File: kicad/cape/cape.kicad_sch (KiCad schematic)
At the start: 13 parts, among them M1 HSR-2648CR, P1 BeagleBone_Black_Header, P2 BeagleBone_Black_Header, SW1 L101011_SPST, U1 L298, U2 BNO055, U3 BMP390, U4 S13V10FS

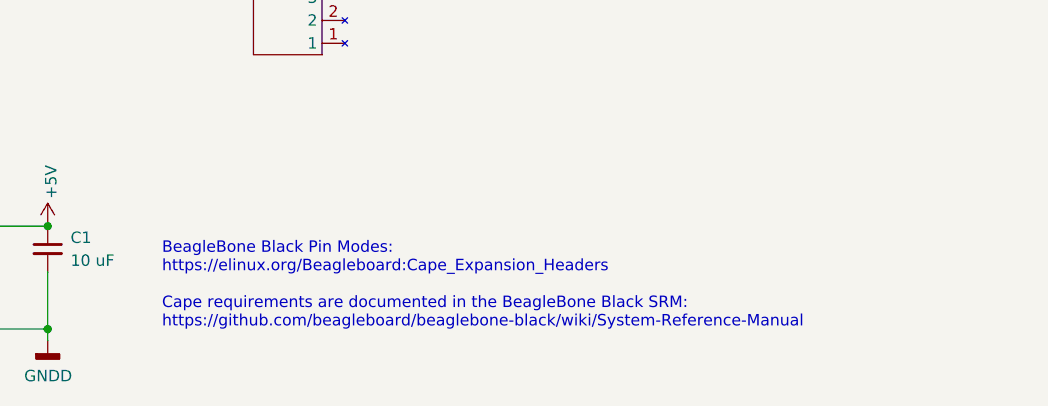
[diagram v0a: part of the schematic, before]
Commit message: Moved cape pdf files to doc
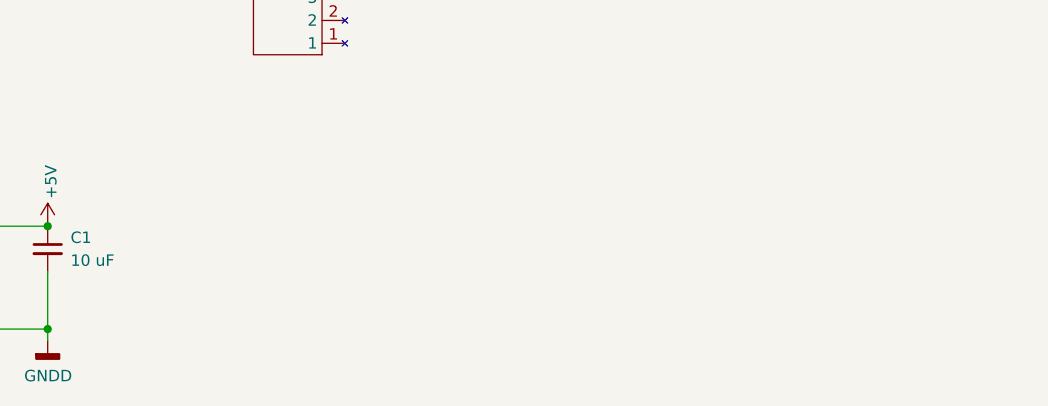
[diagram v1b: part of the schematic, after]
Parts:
- U1: footprint Connector_PinSocket_2.54mm:PinSocket_1x06_P2.54mm_Vertical -> Connector_PinHeader_2.54mm:PinHeader_1x06_P2.54mm_Vertical
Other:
- note removed: "BeagleBone Black Pin Modes: https://elinux.org/Beagleboard:Cape_Expansion_Headers Cape requirements are documented in the BeagleBone Black SRM: https://github.com/beagleboard/beaglebone-black/wiki/System-Reference-Manual"
- title: (none) -> Payload BeagleBone Black Cape
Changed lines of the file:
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@@
 (kicad_sch (version 20211123) (generator eeschema)
   (paper "A4")
+  (title_block
+    (title "Payload BeagleBone Black Cape")
+    (date "2022-12-18")
+    (rev "1.1")
+  )
   (junction (at 134.62 180.34) (diameter 0) (color 0 0 0 0)
   )
@@
     (stroke (width 0) (type default) (color 0 0 0 0))
   )
-  (text "BeagleBone Black Pin Modes:\nhttps://elinux.org/Beagleboard:Cape_Expansion_Headers\n\nCape requirements are documented in the BeagleBone Black SRM:\nhttps://github.com/beagleboard/beaglebone-black/wiki/System-Reference-Manual"
-    (at 177.8 180.34 0)
+  (text "\n" (at 177.8 180.34 0)
     (effects (font (size 1.27 1.27)) (justify left bottom))
   )
@@
     (property "Reference" "U1" (id 0) (at 66.04 124.46 0))
     (property "Value" "L298" (id 1) (at 66.04 127 0))
-    (property "Footprint" "Connector_PinSocket_2.54mm:PinSocket_1x06_P2.54mm_Vertical" (id 2) (at 55.88 129.54 0)
+    (property "Footprint" "Connector_PinHeader_2.54mm:PinHeader_1x06_P2.54mm_Vertical" (id 2) (at 55.88 129.54 0)
       (effects (font (size 1.27 1.27)) hide)
     )
@@
     )
     (path "/ecf7c526-1bd5-49c8-a82a-8acc85e22ee0"
-      (reference "U1") (unit 1) (value "L298") (footprint "Connector_PinSocket_2.54mm:PinSocket_1x06_P2.54mm_Vertical")
+      (reference "U1") (unit 1) (value "L298") (footprint "Connector_PinHeader_2.54mm:PinHeader_1x06_P2.54mm_Vertical")
     )
     (path "/ae4a70ec-7099-49d5-8f39-6daa3b0242a8"

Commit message: Cape v 1.2
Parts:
- removed H1: GPIO_Breakout, Connector_PinHeader_2.54mm:PinHeader_1x08_P2.54mm_Vertical, symbol payload_symbol_library:GPIO_Breakout
- removed U1: L298, Connector_PinHeader_2.54mm:PinHeader_1x06_P2.54mm_Vertical, symbol payload_symbol_library:L298
- removed U3: BMP390, payload_footprint_library:BMP390, symbol payload_symbol_library:BMP390
- added C1: 100 uF, Capacitor_THT:C_Radial_D10.0mm_H16.0mm_P5.00mm, symbol Device:C_Small
- added U3: A4988, payload_footprint_library:Pololu_Breakout-16_15.2x20.3mm, symbol payload_symbol_library:A4988
- C2: renamed from C1; value 10 uF -> 10 nF; footprint Capacitor_THT:C_Radial_D10.0mm_H16.0mm_P5.00mm -> Capacitor_THT:C_Disc_D10.0mm_W2.5mm_P5.00mm
- M1: footprint Connector_PinHeader_2.54mm:PinHeader_1x03_P2.54mm_Vertical -> Connector_PinSocket_2.54mm:PinSocket_1x03_P2.54mm_Vertical
- SW1: footprint payload_footprint_library:SPST -> payload_footprint_library:SW_L101011MS02Q
- U1: renamed from U4; value S13V10FS -> S13V10F5; symbol payload_symbol_library:S13V10FS -> payload_symbol_library:S13V10F5
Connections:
- net +3.3V: now also U3.2 (VDD)
- net +7.4V: now also C1.1, U3.8 (VMOT)
- net GNDD: now also C1.2, U3.1 (GND), U3.7 (GND)
- net GPIO[117]: now also U2.6 (RST)
- net GPIO[20]: no longer U2.6 (RST)
- net GPIO[27]: now also U3.14 (~{SLEEP})
- net GPIO[47]: now also U3.13 (~{RESET})
- net GPIO[61]: now also U3.16 (DIR)
- net GPIO[65]: now also U3.15 (STEP)
- net I2C2.SCL: now also R2.2; no longer R1.2
- net I2C2.SDA: now also R1.2; no longer R2.2
- net GPIO[122] renamed GPIO_112
- net GPIO_112: now also U2.9 (INT)
- net GPIO[125] renamed GPIO_115
- no-connect marks 0 -> 12
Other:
- moved on the sheet: BT1, C2, M1, P1, P2, SW1, U1

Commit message: Cape 1.3, Main 1.7
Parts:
- added C3: 100 uF, Capacitor_THT:C_Radial_D10.0mm_H16.0mm_P5.00mm, symbol Device:C_Small
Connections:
- net +5V: now also C3.1
- net GNDD: now also C3.2
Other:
- moved on the sheet: BT1, C1, C2, M1, P1, P2, R1, R2, SW1, U1, U2, U3

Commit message: Updated all schematics
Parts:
- removed SW1: L101011_SPST, payload_footprint_library:SW_L101011MS02Q, symbol Switch:SW_SPST
- added JP1: Jumper_3_Open, Connector_PinHeader_2.54mm:PinHeader_1x03_P2.54mm_Vertical, symbol Jumper:Jumper_3_Open
- added U3: stepper_breakout, Connector_PinSocket_2.54mm:PinSocket_1x04_P2.54mm_Vertical, symbol payload_symbol_library:stepper_breakout
- renumbered U2 to U1, U1 to U2, U3 to U4
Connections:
- net +7.4V: now also JP1.3 (B)
- net at BT1.1 (+): now also JP1.2 (C)
- net at U4.3 (1B): now also U3.1 (1B)
- net at U4.4 (1A): now also U3.2 (1A)
- net at U4.5 (2A): now also U3.3 (2A)
- net at U4.6 (2B): now also U3.4 (2B)
- no-connect marks 12 -> 9
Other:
- company: (none) -> Peter Costescu
- moved on the sheet: U4

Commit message: Exported gerber to JLC PCB
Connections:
- net GPIO[61]: now also P2.26 (Pin_26); no longer P2.28 (Pin_28)
- net LCD.PCLK: now also P2.28 (Pin_28); no longer P2.26 (Pin_26)
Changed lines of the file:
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@@
+    (effects (font (size 1.27 1.27)) (justify right bottom))
+  )
+  (label "LCD.PCLK" (at 129.54 60.96 180)
     (effects (font (size 1.27 1.27)) (justify right bottom))
   )
@@
     (effects (font (size 1.27 1.27)) (justify left bottom))
   )
-  (label "LCD.PCLK" (at 129.54 58.42 180)
-    (effects (font (size 1.27 1.27)) (justify right bottom))
-  )
   (label "GPIO[44]" (at 129.54 40.64 180)
     (effects (font (size 1.27 1.27)) (justify right bottom))
@@
     (effects (font (size 1.27 1.27)) (justify left bottom))
   )
-  (label "GPIO[61]" (at 129.54 60.96 180)
-    (effects (font (size 1.27 1.27)) (justify right bottom))
-  )
   (label "GPIO_112" (at 67.31 63.5 180)
     (effects (font (size 1.27 1.27)) (justify right bottom))
@@
     (effects (font (size 1.27 1.27)) (justify right bottom))
   )
+  (label "GPIO[61]" (at 129.54 58.42 180)
+    (effects (font (size 1.27 1.27)) (justify right bottom))
+  )

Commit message: Working on post-build payload changes
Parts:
- removed U3: stepper_breakout, Connector_PinSocket_2.54mm:PinSocket_1x04_P2.54mm_Vertical, symbol payload_symbol_library:stepper_breakout
- removed U4: A4988, payload_footprint_library:Pololu_Breakout-16_15.2x20.3mm, symbol payload_symbol_library:A4988
- added C4: 220 uF, Capacitor_THT:C_Radial_D8.0mm_H7.0mm_P3.50mm, symbol Device:C_Small
- added M? (x2): Motor_Servo_Feedback, symbol payload_symbol_library:Motor_Servo_Feedback
- C1: value 100 uF -> 220 uF; footprint Capacitor_THT:C_Radial_D10.0mm_H16.0mm_P5.00mm -> Capacitor_THT:C_Radial_D8.0mm_H11.5mm_P3.50mm
- C3: value 100 uF -> 220 uF; footprint Capacitor_THT:C_Radial_D10.0mm_H16.0mm_P5.00mm -> Capacitor_THT:C_Radial_D8.0mm_H7.0mm_P3.50mm
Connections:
- net +5V: now also C4.1
- net +7.4V: now also M?.2 (+)
- net GNDD: now also C4.2, M?.3 (-); no longer P2.45 (Pin_45)
- net GPIO[23]: now also M?.1 (PWM); no longer P2.13 (Pin_13)
- net GPIO[22] renamed PWM2A
- net GPIO[40] renamed PWM1A
- net GPIO[51] renamed PWM1B
- net LCD.DATA[0] renamed LCD_DATA2
- net LCD.DATA[2] renamed LCD_DATA4
- net LCD.DATA[4] renamed LCD_DATA6
- net LCD.DATA[6] renamed LCD_DATA8
- net LCD.DATA[8] renamed LCD_DATA12
- new net LCD_DATA0: P2.45 (Pin_45)
- new net PWM2B: P2.13 (Pin_13)
- no-connect marks 9 -> 5
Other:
- moved on the sheet: M1

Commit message: Cape v1-5
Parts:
- removed M1: HSR-2648CR, Connector_PinSocket_2.54mm:PinSocket_1x03_P2.54mm_Vertical, symbol Motor:Motor_Servo
- M1, M2: renamed from M?; footprint (none) -> Connector_PinHeader_2.54mm:PinHeader_1x04_P2.54mm_Vertical
- R1, R2: footprint Resistor_THT:R_Axial_DIN0207_L6.3mm_D2.5mm_P10.16mm_Horizontal -> Resistor_THT:R_Axial_DIN0207_L6.3mm_D2.5mm_P15.24mm_Horizontal
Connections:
- net GPIO[23] is gone; now on net PWM2B: M2.1 (PWM)
- net +7.4V: now also M1.2 (+)
- net GNDD: now also M1.3 (-)
- net GPIO[27]: now also M1.4 (FDBK)
- net GPIO[45]: now also M2.4 (FDBK)
- net PWM2A: now also M1.1 (PWM)

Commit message: Cape v1-5
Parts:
- added D?: 1N5817, Diode_THT:D_DO-41_SOD81_P10.16mm_Horizontal, symbol Diode:1N5817
- U2: value S13V10F5 -> S13V20F5
- renumbered P2 to P8, P1 to P9
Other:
- note added: "Body Tube"
- note added: "Camera"
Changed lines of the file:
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@@
   (title_block
     (title "Payload BeagleBone Black Cape")
-    (date "2022-12-30")
-    (rev "1.4")
+    (date "2023-02-17")
+    (rev "1.5")
     (company "Peter Costescu")
   )
@@
     (effects (font (size 1.27 1.27)) (justify left bottom))
   )
+  (text "Camera" (at 163.83 95.25 0)
+    (effects (font (size 1.27 1.27)) (justify left bottom))
+  )
+  (text "Body Tube" (at 163.83 78.74 0)
+    (effects (font (size 1.27 1.27)) (justify left bottom))
+  )
   (label "GPIO[45]" (at 78.74 40.64 0)
     (effects (font (size 1.27 1.27)) (justify left bottom))
@@
   (symbol (lib_id "Connector_Generic:Conn_02x23_Odd_Even") (at 40.64 55.88 0) (unit 1)
     (in_bom yes) (on_board yes)
-    (property "Reference" "P1" (id 0) (at 41.91 25.4 0))
+    (property "Reference" "P9" (id 0) (at 41.91 25.4 0))
     (property "Value" "BeagleBone_Black_Header" (id 1) (at 41.91 54.61 90)
       (effects (font (size 1.27 1.27)) hide)
@@
   (symbol (lib_id "Connector_Generic:Conn_02x23_Odd_Even") (at 102.87 55.88 0) (unit 1)
     (in_bom yes) (on_board yes)
-    (property "Reference" "P2" (id 0) (at 104.14 25.4 0))
+    (property "Reference" "P8" (id 0) (at 104.14 25.4 0))
     (property "Value" "BeagleBone_Black_Header" (id 1) (at 104.14 54.61 90)
       (effects (font (size 1.27 1.27)) hide)
@@
     (pin "2")
   )
+  (symbol (lib_id "Diode:1N5817") (at 46.99 114.3 0) (unit 1)
+    (in_bom yes) (on_board yes) (fields_autoplaced)
+    (property "Reference" "D?" (id 0) (at 46.6725 107.95 0))
+    (property "Value" "1N5817" (id 1) (at 46.6725 110.49 0))
+    (property "Footprint" "Diode_THT:D_DO-41_SOD81_P10.16mm_Horizontal" (id 2) (at 46.99 118.745 0)
+      (effects (font (size 1.27 1.27)) hide)
+    )
+    (property "Datasheet" "http://www.vishay.com/docs/88525/1n5817.pdf" (id 3) (at 46.99 114.3 0)
+      (effects (font (size 1.27 1.27)) hide)
+    )
+    (pin "1")
+    (pin "2")
+  )
   (symbol (lib_id "payload_symbol_library:S13V10F5") (at 86.36 104.14 0) (unit 1)
     (in_bom yes) (on_board yes) (fields_autoplaced)
     (property "Reference" "U2" (id 0) (at 78.74 99.06 0))
-    (property "Value" "S13V10F5" (id 1) (at 78.74 101.6 0))
+    (property "Value" "S13V20F5" (id 1) (at 78.74 101.6 0))
     (property "Footprint" "payload_footprint_library:S13V10F5" (id 2) (at 86.36 104.14 0)
       (effects (font (size 1.27 1.27)) hide)
@@
       (reference "C4") (unit 1) (value "220 uF") (footprint "Capacitor_THT:C_Radial_D8.0mm_H7.0mm_P3.50mm")
     )
+    (path "/6bb30dad-d00d-4f24-bbf3-1a5123f9cf09"
+      (reference "D?") (unit 1) (value "1N5817") (footprint "Diode_THT:D_DO-41_SOD81_P10.16mm_Horizontal")
+    )
     (path "/726ef827-8827-493f-9c4b-ec50e711c458"
       (reference "JP1") (unit 1) (value "Jumper_3_Open") (footprint "Connector_PinHeader_2.54mm:PinHeader_1x03_P2.54mm_Vertical")
@@
       (reference "M2") (unit 1) (value "Motor_Servo_Feedback") (footprint "Connector_PinHeader_2.54mm:PinHeader_1x04_P2.54mm_Vertical")
     )
+    (path "/00000000-0000-0000-0000-000055df7de1"
+      (reference "P8") (unit 1) (value "BeagleBone_Black_Header") (footprint "Connector_PinHeader_2.54mm:PinHeader_2x23_P2.54mm_Vertical")
+    )
     (path "/00000000-0000-0000-0000-000055df7dba"
-      (reference "P1") (unit 1) (value "BeagleBone_Black_Header") (footprint "Connector_PinHeader_2.54mm:PinHeader_2x23_P2.54mm_Vertical")
-    )
-    (path "/00000000-0000-0000-0000-000055df7de1"
-      (reference "P2") (unit 1) (value "BeagleBone_Black_Header") (footprint "Connector_PinHeader_2.54mm:PinHeader_2x23_P2.54mm_Vertical")
+      (reference "P9") (unit 1) (value "BeagleBone_Black_Header") (footprint "Connector_PinHeader_2.54mm:PinHeader_2x23_P2.54mm_Vertical")
     )
     (path "/ee1b16ae-e588-46d6-aa69-d0431f2f57f1"
@@
     )
     (path "/6c4e6561-0632-4611-9af2-438014839037"
-      (reference "U2") (unit 1) (value "S13V10F5") (footprint "payload_footprint_library:S13V10F5")
-    )
-  )
+      (reference "U2") (unit 1) (value "S13V20F5") (footprint "payload_footprint_library:S13V10F5")
+    )
+  )
